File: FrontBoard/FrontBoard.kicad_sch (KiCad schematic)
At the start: 34 parts

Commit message: corrected duplicate annotations, simplified signal path, passes all DRC checks
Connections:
- net C2MixIn1 is gone; now on net Signal1: R5.1
- net C2MixIn2 is gone; now on net Signal2: R6.1
- net C2MixIn3 is gone; now on net Signal3: R7.1
- net C2MixIn4 is gone; now on net Signal4: R8.1
- net C3MixIn1 is gone; now on net Signal1: R9.1
- net C3MixIn2 is gone; now on net Signal2: R10.1
- net C3MixIn3 is gone; now on net Signal3: R11.1
- net C3MixIn4 is gone; now on net Signal4: R12.1
- net C1MixIn1 renamed Signal1
- net C1MixIn2 renamed Signal2
- net C1MixIn3 renamed Signal3
- net C1MixIn4 renamed Signal4
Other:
- company: (none) -> R-mods
- title: (none) -> Matrix Mixer

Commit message: assigned some footprints
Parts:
- R1, R10, R11, R12, R2, R3, R4, R5, R6, R7, R8, R9: footprint (none) -> Resistor_THT:R_Axial_DIN0207_L6.3mm_D2.5mm_P10.16mm_Horizontal
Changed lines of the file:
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@@
       (effects (font (size 1.27 1.27)))
     )
-    (property "Footprint" "" (at 160.655 55.753 90)
+    (property "Footprint" "Resistor_THT:R_Axial_DIN0207_L6.3mm_D2.5mm_P10.16mm_Horizontal" (at 160.655 55.753 90)
       (effects (font (size 1.27 1.27)) hide)
     )
@@
       (effects (font (size 1.27 1.27)))
     )
-    (property "Footprint" "" (at 227.965 84.328 90)
+    (property "Footprint" "Resistor_THT:R_Axial_DIN0207_L6.3mm_D2.5mm_P10.16mm_Horizontal" (at 227.965 84.328 90)
       (effects (font (size 1.27 1.27)) hide)
     )
@@
       (effects (font (size 1.27 1.27)))
     )
-    (property "Footprint" "" (at 160.655 84.328 90)
+    (property "Footprint" "Resistor_THT:R_Axial_DIN0207_L6.3mm_D2.5mm_P10.16mm_Horizontal" (at 160.655 84.328 90)
       (effects (font (size 1.27 1.27)) hide)
     )
@@
       (effects (font (size 1.27 1.27)))
     )
-    (property "Footprint" "" (at 227.965 65.913 90)
+    (property "Footprint" "Resistor_THT:R_Axial_DIN0207_L6.3mm_D2.5mm_P10.16mm_Horizontal" (at 227.965 65.913 90)
       (effects (font (size 1.27 1.27)) hide)
     )
@@
       (effects (font (size 1.27 1.27)))
     )
-    (property "Footprint" "" (at 227.965 75.438 90)
+    (property "Footprint" "Resistor_THT:R_Axial_DIN0207_L6.3mm_D2.5mm_P10.16mm_Horizontal" (at 227.965 75.438 90)
       (effects (font (size 1.27 1.27)) hide)
     )
@@
       (effects (font (size 1.27 1.27)))
     )
-    (property "Footprint" "" (at 160.655 74.803 90)
+    (property "Footprint" "Resistor_THT:R_Axial_DIN0207_L6.3mm_D2.5mm_P10.16mm_Horizontal" (at 160.655 74.803 90)
       (effects (font (size 1.27 1.27)) hide)
     )
@@
       (effects (font (size 1.27 1.27)))
     )
-    (property "Footprint" "" (at 160.655 65.278 90)
+    (property "Footprint" "Resistor_THT:R_Axial_DIN0207_L6.3mm_D2.5mm_P10.16mm_Horizontal" (at 160.655 65.278 90)
       (effects (font (size 1.27 1.27)) hide)
     )
@@
       (effects (font (size 1.27 1.27)))
     )
-    (property "Footprint" "" (at 93.98 55.753 90)
+    (property "Footprint" "Resistor_THT:R_Axial_DIN0207_L6.3mm_D2.5mm_P10.16mm_Horizontal" (at 93.98 55.753 90)
       (effects (font (size 1.27 1.27)) hide)
     )
@@
       (effects (font (size 1.27 1.27)))
     )
-    (property "Footprint" "" (at 93.98 84.328 90)
+    (property "Footprint" "Resistor_THT:R_Axial_DIN0207_L6.3mm_D2.5mm_P10.16mm_Horizontal" (at 93.98 84.328 90)
       (effects (font (size 1.27 1.27)) hide)
     )
@@
       (effects (font (size 1.27 1.27)))
     )
-    (property "Footprint" "" (at 93.98 65.278 90)
+    (property "Footprint" "Resistor_THT:R_Axial_DIN0207_L6.3mm_D2.5mm_P10.16mm_Horizontal" (at 93.98 65.278 90)
       (effects (font (size 1.27 1.27)) hide)
     )
@@
       (effects (font (size 1.27 1.27)))
     )
-    (property "Footprint" "" (at 227.965 56.388 90)
+    (property "Footprint" "Resistor_THT:R_Axial_DIN0207_L6.3mm_D2.5mm_P10.16mm_Horizontal" (at 227.965 56.388 90)
       (effects (font (size 1.27 1.27)) hide)
     )
@@
       (effects (font (size 1.27 1.27)))
     )
-    (property "Footprint" "" (at 93.98 74.803 90)
+    (property "Footprint" "Resistor_THT:R_Axial_DIN0207_L6.3mm_D2.5mm_P10.16mm_Horizontal" (at 93.98 74.803 90)
       (effects (font (size 1.27 1.27)) hide)
     )
@@
     )
   )
+  (sheet_instances
+    (path "/" (page "1"))
+  )
 )

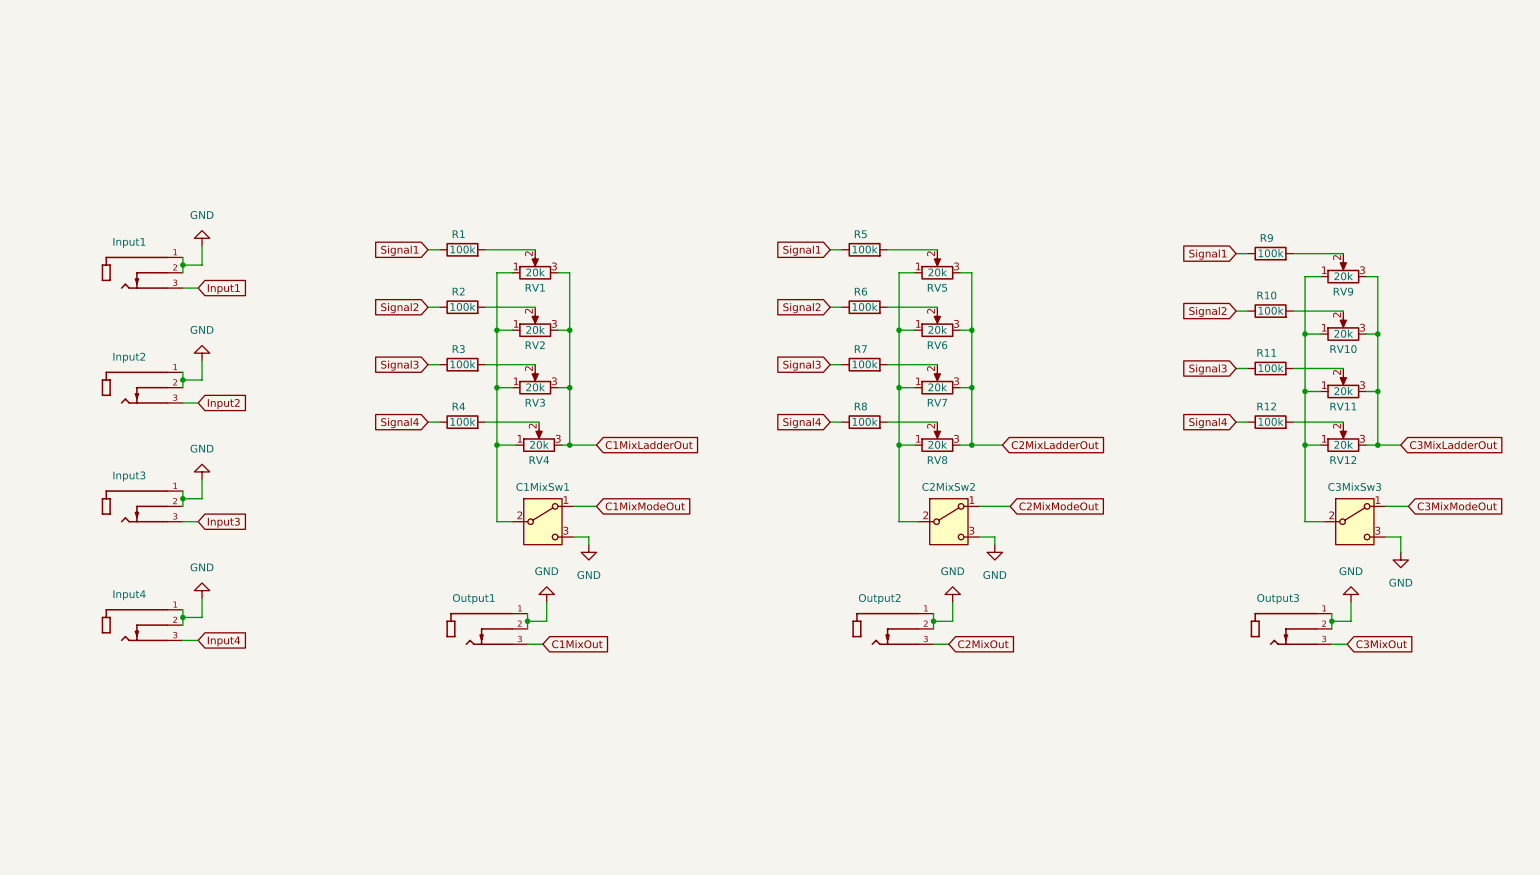
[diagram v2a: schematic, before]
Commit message: added footprints and 3dmodels
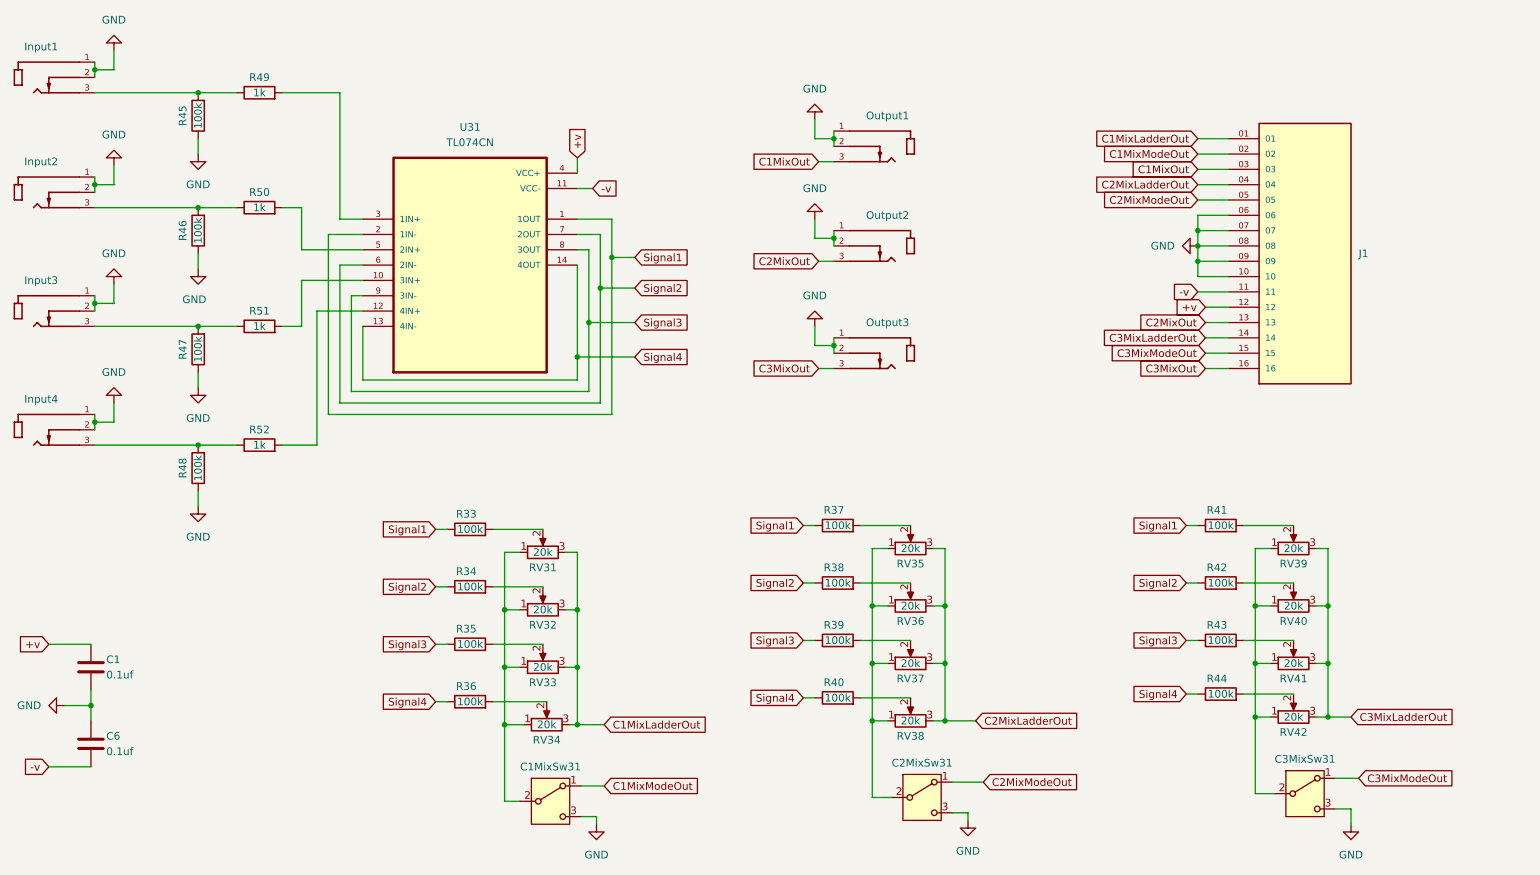
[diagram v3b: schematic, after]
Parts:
- removed C1MixSw1, C2MixSw2, C3MixSw3: SW_SPDT, symbol Switch:SW_SPDT
- removed R1, R10, R11, R12, R2, R3, R4, R5, R6, R7, R8, R9: 100k, Resistor_THT:R_Axial_DIN0207_L6.3mm_D2.5mm_P10.16mm_Horizontal, symbol Device:R
- removed RV1, RV10, RV11, RV12, RV2, RV3, RV4, RV5, RV6, RV7, RV8, RV9: 20k, symbol Device:R_Potentiometer
- added C1, C6: 0.1uf, Capacitor_THT:C_Disc_D7.5mm_W4.4mm_P5.00mm, symbol Device:C
- added C1MixSw31, C2MixSw31, C3MixSw31: SW_SPDT, 100SP1T6B11M1REH:SW_100SP1T6B11M1REH, symbol Switch:SW_SPDT
- added J1: ESQ-116-33-L-S, ESQ-116-33-L-S:SAMTEC_ESQ-116-33-L-S, symbol ESQ-116-33-L-S:ESQ-116-33-L-S
- added R33, R34, R35, R36, R37, R38, R39, R40, R41, R42, R43, R44, R45, R46, R47, R48: 100k, Resistor_THT:R_Axial_DIN0207_L6.3mm_D2.5mm_P10.16mm_Horizontal, symbol Device:R
- added R49, R50, R51, R52: 1k, Resistor_THT:R_Axial_DIN0207_L6.3mm_D2.5mm_P10.16mm_Horizontal, symbol Device:R
- added RV31, RV32, RV33, RV34, RV35, RV36, RV37, RV38, RV39, RV40, RV41, RV42: 20k, Potentiometer_THT:Potentiometer_TT_P0915N, symbol Device:R_Potentiometer
- added U31: TL074CN, TL074CN:DIP794W45P254L1969H508Q14, symbol TL074CN:TL074CN
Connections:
- net C1MixLadderOut: now also J1.01, RV31.3, RV32.3, RV33.3, RV34.3
- net C1MixModeOut: now also C1MixSw31.1 (A), J1.02
- net C1MixOut: now also J1.03
- net C2MixLadderOut: now also J1.04, RV35.3, RV36.3, RV37.3, RV38.3
- net C2MixModeOut: now also C2MixSw31.1 (A), J1.05
- net C2MixOut: now also J1.13
- net C3MixLadderOut: now also J1.14, RV39.3, RV40.3, RV41.3, RV42.3
- net C3MixModeOut: now also C3MixSw31.1 (A), J1.15
- net C3MixOut: now also J1.16
- net GND: now also C1.2, C1MixSw31.3 (C), C2MixSw31.3 (C), C3MixSw31.3 (C), C6.2, J1.06, J1.07, J1.08, J1.09, J1.10, R45.1, R46.1, R47.1, R48.1
- net Signal1: now also R33.1, R37.1, R41.1, U31.1 (1OUT), U31.2 (1IN-)
- net Signal2: now also R34.1, R38.1, R42.1, U31.6 (2IN-), U31.7 (2OUT)
- net Signal3: now also R35.1, R39.1, R43.1, U31.8 (3OUT), U31.9 (3IN-)
- net Signal4: now also R36.1, R40.1, R44.1, U31.13 (4IN-), U31.14 (4OUT)
- net Input1: no longer names the net of Input1.3
- net Input1: now also R45.2, R49.1
- net Input2: no longer names the net of Input2.3
- net Input2: now also R46.2, R50.1
- net Input3: no longer names the net of Input3.3
- net Input3: now also R47.2, R51.1
- net Input4: no longer names the net of Input4.3
- net Input4: now also R48.2, R52.1
- new net: R39.2, RV37.2
- new net: R37.2, RV35.2
- new net: C3MixSw31.2 (B), RV39.1, RV40.1, RV41.1, RV42.1
- new net: R41.2, RV39.2
- new net: R35.2, RV33.2
- new net: R44.2, RV42.2
- new net: C2MixSw31.2 (B), RV35.1, RV36.1, RV37.1, RV38.1
- new net: R42.2, RV40.2
- new net: R43.2, RV41.2
- new net: R51.2, U31.10 (3IN+)
- new net: C1MixSw31.2 (B), RV31.1, RV32.1, RV33.1, RV34.1
- new net: R33.2, RV31.2
- new net: R36.2, RV34.2
- new net: R34.2, RV32.2
- new net: R49.2, U31.3 (1IN+)
- new net: R40.2, RV38.2
- new net: R38.2, RV36.2
- new net: R52.2, U31.12 (4IN+)
- new net: R50.2, U31.5 (2IN+)
- new net +v: C1.1, J1.12, U31.4 (VCC+)
- new net -v: C6.1, J1.11, U31.11 (VCC-)
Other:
- moved on the sheet: Input1, Input2, Input3, Input4
